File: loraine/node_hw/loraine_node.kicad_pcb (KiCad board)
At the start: 2 copper layers, 50.8 x 53.3 mm, 32 parts, among them CON1 BARREL_JACK, IC1 ATTINY2313A-S, P1 MOLEX, P2 MOLEX, P4 ICSP, P5 OUTPUTS, P6 BUS, P7 BUS_THRU, Q1 BD679, Q2 BD679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

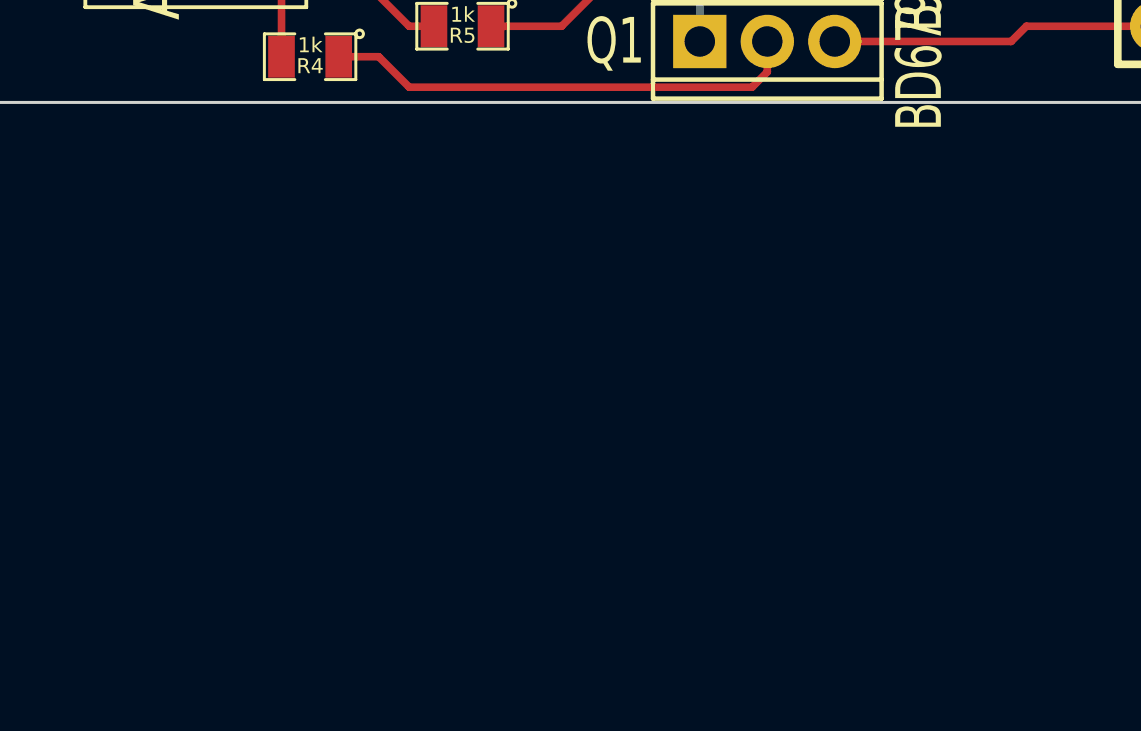
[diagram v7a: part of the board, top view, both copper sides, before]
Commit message: Added remaining footprints to netlist/pcb
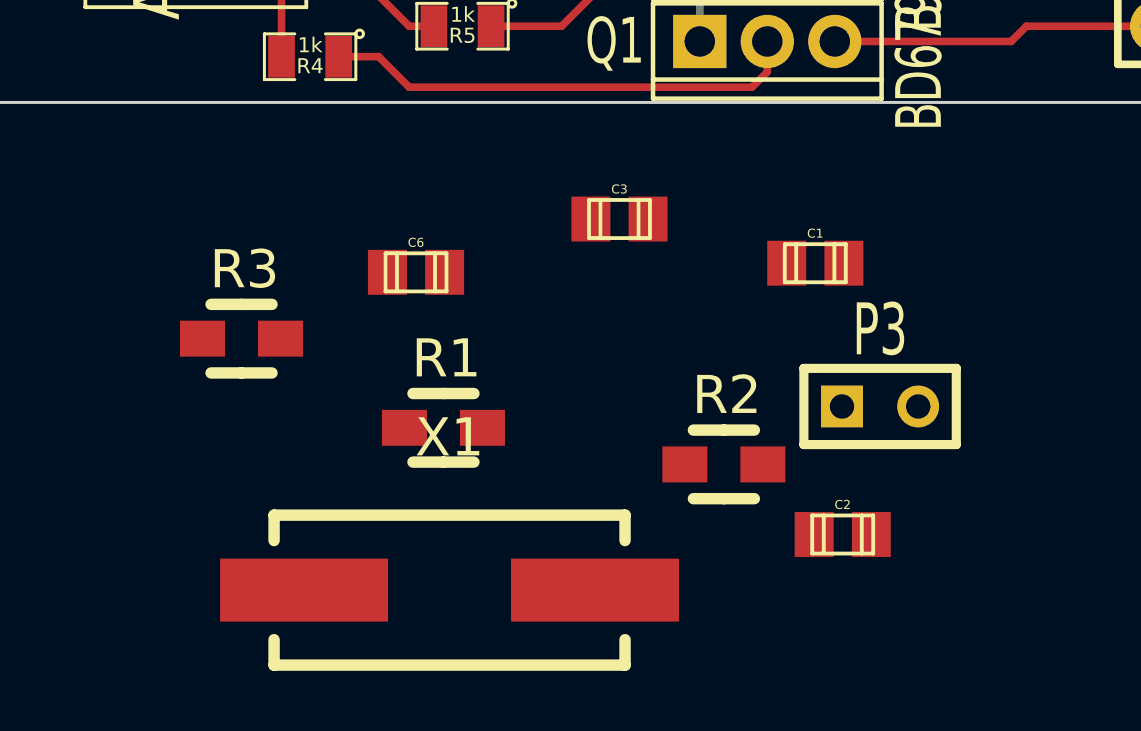
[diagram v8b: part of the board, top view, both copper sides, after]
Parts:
- added C1: 0.33uF, Capacitors_SMD:c_0805, F.Cu at (83.6, 109.5)
- added C2: 0.1uF, Capacitors_SMD:c_0805, F.Cu at (84.6, 118.5)
- added C3: 0.1uF, Capacitors_SMD:c_0805, F.Cu at (77.1, 108.0)
- added C6: 0.1uF, Capacitors_SMD:c_0805, F.Cu at (70.3, 109.8)
- added P3: SOLDER_PAD, Connect:SIL-2, F.Cu at (85.8, 114.3)
- added R1: 0.47R 0.25W, Resistors_SMD:Resistor_SMD0805_HandSoldering, F.Cu at (71.2, 115.0)
- added R2: 0.47R 0.25W, Resistors_SMD:Resistor_SMD0805_HandSoldering, F.Cu at (80.6, 116.2)
- added R3: 0.47R 0.25W, Resistors_SMD:Resistor_SMD0805_HandSoldering, F.Cu at (64.5, 112.0)
- added X1: 16MHz, Crystals:Crystal_HC49-SD_SMD, F.Cu at (71.5, 120.4)
